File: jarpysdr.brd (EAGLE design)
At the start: 90 x 45 mm, 37 parts, among them IC1 74HC74N, IC2 NE5532N, IC3 7805, IC4 TL072P

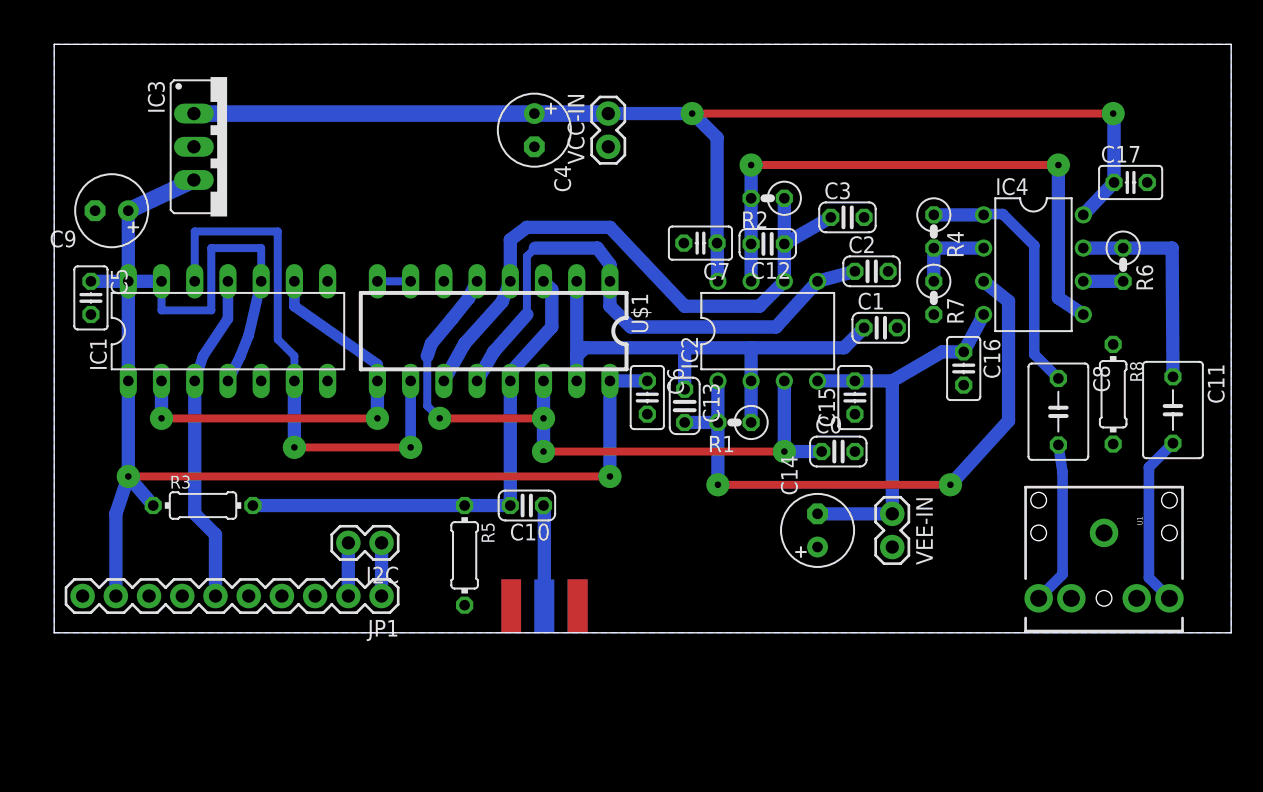
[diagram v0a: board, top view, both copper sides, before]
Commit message: Re-align all parts to a 0.1inch grid.
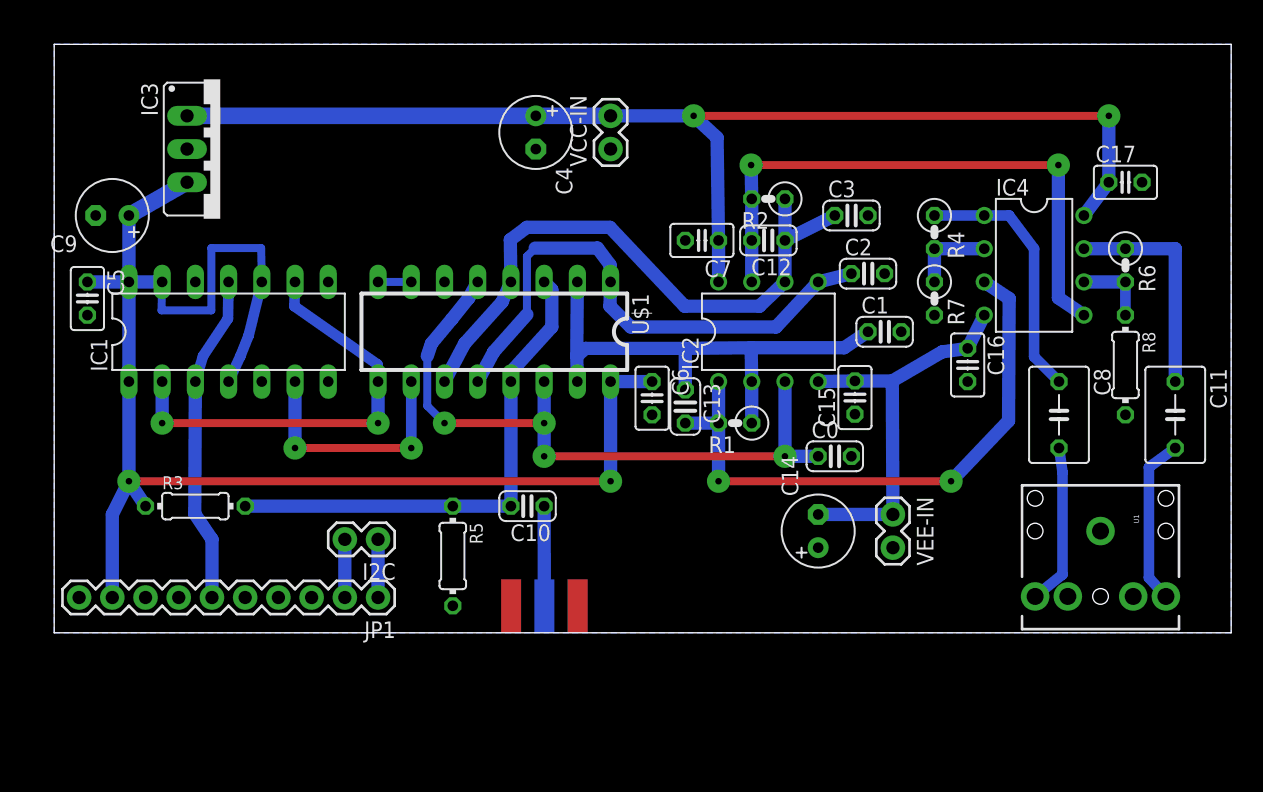
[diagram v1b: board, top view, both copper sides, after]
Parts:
- moved R8 2.43 mm to (81.9, 30.5)
- moved R5 0.91 mm to (30.5, 15.9)
- moved R3 0.59 mm to (10.8, 19.7)
- moved IC3 0.55 mm to (12.7, 47.0)
- moved C0 0.45 mm to (59.7, 23.5)
- moved C1 0.43 mm to (63.5, 33.0)
- moved C16 0.40 mm to (69.8, 30.5)
- moved C11 0.40 mm to (85.7, 26.7)
- moved C17 0.40 mm to (81.9, 44.5)
- moved I2C 0.38 mm to (24.8, 17.1)
- moved C9 0.37 mm to (4.45, 41.9)
- moved C6 0.37 mm to (45.7, 27.9)
- moved C3 0.33 mm to (61.0, 41.9)
- moved C2 0.32 mm to (62.2, 37.5)
- moved U1 0.31 mm to (80.0, 17.8)
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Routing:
- net N$3: track 41.2 -> 19.1 mm
- net N$15: track 3.05 -> 5.72 mm
- net N$2: track 33.2 -> 33.8 mm
- net N$4: track 38.3 -> 38.9 mm
- net +12V: track 92.8 -> 92.2 mm
- net N$13: track 16.6 -> 17.1 mm

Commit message: Double-sided layout.
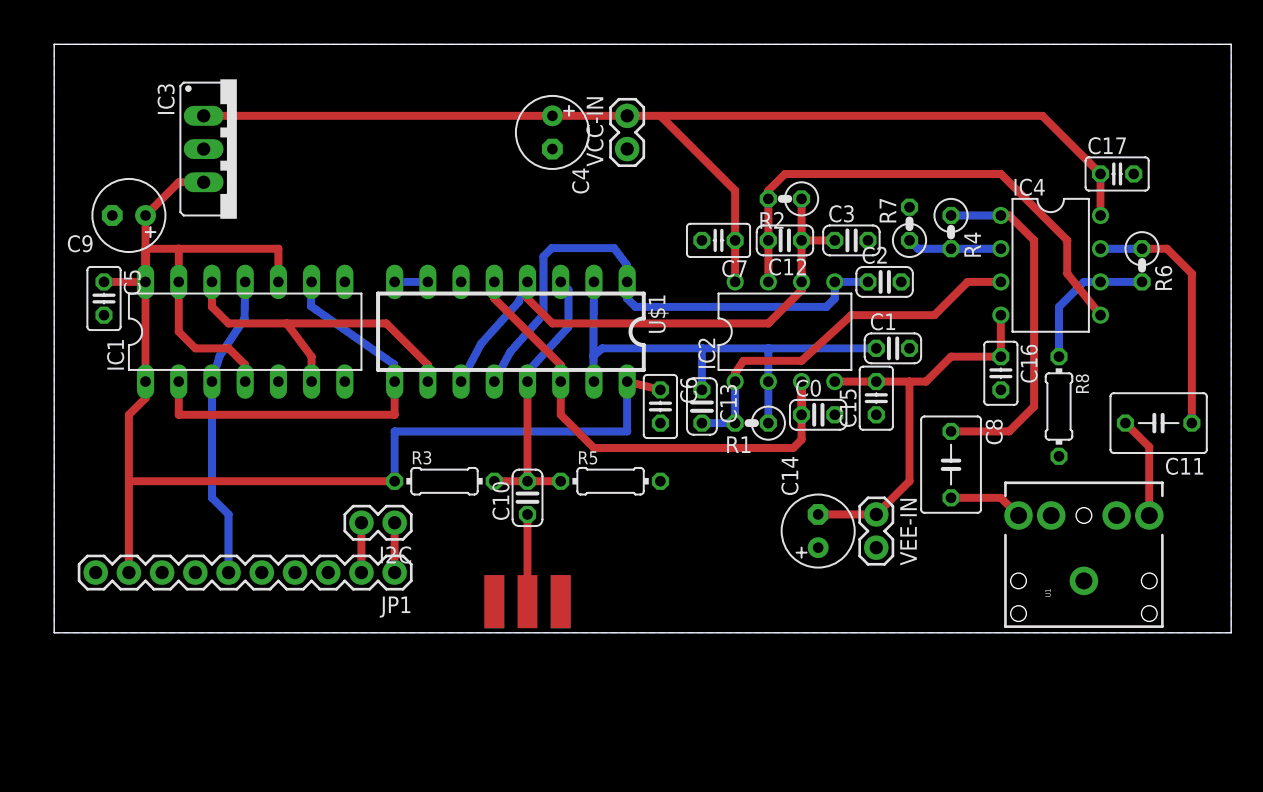
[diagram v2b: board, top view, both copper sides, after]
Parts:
- moved R3 19.1 mm to (29.8, 21.6)
- moved R5 13.4 mm to (42.5, 21.6), turned to 0 degrees
- moved C8 9.09 mm to (68.6, 22.9)
- moved R7 6.02 mm to (65.4, 41.3), turned to 90 degrees
- moved R8 5.99 mm to (76.8, 27.3)
- moved U1 4.02 mm to (78.7, 14.0), turned to 90 degrees
- moved J$1 3.81 mm to (38.7, 12.4), flipped to the top
- moved C0 3.42 mm to (58.4, 26.7)
- moved C16 2.62 mm to (72.4, 29.8)
- moved JP1 2.29 mm to (26.0, 14.6)
- moved C3 1.90 mm to (61.0, 40.0)
- moved I2C 1.80 mm to (26.0, 18.4)
- moved C15 1.64 mm to (62.9, 27.9)
- moved C1 1.42 mm to (64.1, 31.8)
- moved C2 1.42 mm to (63.5, 36.8)
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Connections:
- net GND: now also J$1.GND@2, J$1.GND@3
- net N$8: now also U1.TIP; no longer U1.RING
- net N$9: now also U1.RING; no longer U1.TIP
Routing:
- net N$4: track 38.9 -> 21.8 mm
- net N$6: track 46.0 -> 29.6 mm, vias 2 -> 0
- net N$5: track 52.6 -> 39.0 mm, vias 4 -> 0
- net N$3: track 19.1 -> 26.6 mm, vias 2 -> 0
- net N$11: track 19.8 -> 27.0 mm
- net N$9: track 12.4 -> 5.72 mm
- net N$10: track 44.9 -> 39.1 mm, vias 2 -> 0
- net N$15: track 5.72 -> 10.9 mm
- net N$8: track 12.9 -> 7.82 mm
- net N$14: track 47.7 -> 42.8 mm
- net +12V: track 92.2 -> 88.7 mm, vias 2 -> 0
- net N$13: track 17.1 -> 19.2 mm
- net CLK: track 25.2 -> 23.4 mm
- net +5V: track 115.5 -> 113.8 mm, vias 2 -> 0
- net -12V: track 30.8 -> 32.3 mm
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
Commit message: Move osc connector to left edge.
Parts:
- moved VCC-IN 42.3 mm to (1.59, 49.8)
- moved C4 30.6 mm to (7.62, 51.1)
- moved JP1 24.8 mm to (1.59, 19.1), turned to 90 degrees
- moved I2C 24.8 mm to (1.59, 14.3), turned to 270 degrees
- moved IC3 5.71 mm to (19.7, 47.0)
- moved C14 4.02 mm to (59.7, 21.6), turned to 0 degrees
- moved R5 3.62 mm to (44.8, 18.7)
- moved C10 3.43 mm to (38.1, 17.5)
- moved VEE-IN 3.17 mm to (64.8, 21.6)
- moved R3 2.13 mm to (31.8, 22.5), turned to 270 degrees
- moved C0 1.91 mm to (60.3, 26.7)
- moved C1 1.91 mm to (66.0, 31.8)
- moved C11 1.91 mm to (86.4, 26.0)
- moved C13 1.91 mm to (51.4, 27.3)
- moved C16 1.91 mm to (74.3, 29.8)
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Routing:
- net +12V: track 88.7 -> 101.6 mm
- net +5V: track 113.8 -> 103.5 mm
- net N$17: track 3.81 -> 13.7 mm
- net N$4: track 21.8 -> 28.8 mm
- net N$7: track 6.67 -> 3.81 mm
- net -12V: track 32.3 -> 30.6 mm
- net N$16: track 3.81 -> 4.76 mm
- net N$3: track 26.6 -> 26.0 mm
- net CLK: track 23.4 -> 22.9 mm

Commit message: Gave some love to the ground plane.
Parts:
- moved I2C 9.16 mm to (10.5, 12.1), turned to 0 degrees
- moved C16 3.59 mm to (71.8, 32.4), turned to 90 degrees
- moved C17 2.54 mm to (80.6, 45.1), turned to 180 degrees
- moved C3 1.59 mm to (61.9, 41.3), turned to 90 degrees
- moved C2 1.42 mm to (64.8, 38.1), turned to 90 degrees
- moved R7 1.14 mm to (68.3, 40.6)
- moved C6 0.71 mm to (48.6, 27.9)
- moved R4 0.64 mm to (71.1, 40.6)
- moved C13 0.64 mm to (51.4, 27.9)
- moved R1 0.64 mm to (55.2, 26.7)
- moved JP1 0.64 mm to (2.22, 19.1)
- moved VCC-IN 0.64 mm to (2.22, 49.8)
- moved C1 0.45 mm to (65.7, 32.1)
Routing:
- net N$16: track 4.76 -> 12.1 mm
- net N$1: track 40.8 -> 45.9 mm
- net N$17: track 13.7 -> 16.0 mm
- net -12V: track 30.6 -> 29.0 mm
- net N$12: track 7.25 -> 6.03 mm
- net N$14: track 42.8 -> 43.9 mm
- net C-180DEG: track 38.4 -> 37.4 mm
- net N$5: track 39.0 -> 39.7 mm
- net N$11: track 27.0 -> 26.3 mm
- net N$6: track 29.6 -> 29.0 mm
- net CLK: track 22.9 -> 22.2 mm
- net +12V: track 101.6 -> 101.0 mm

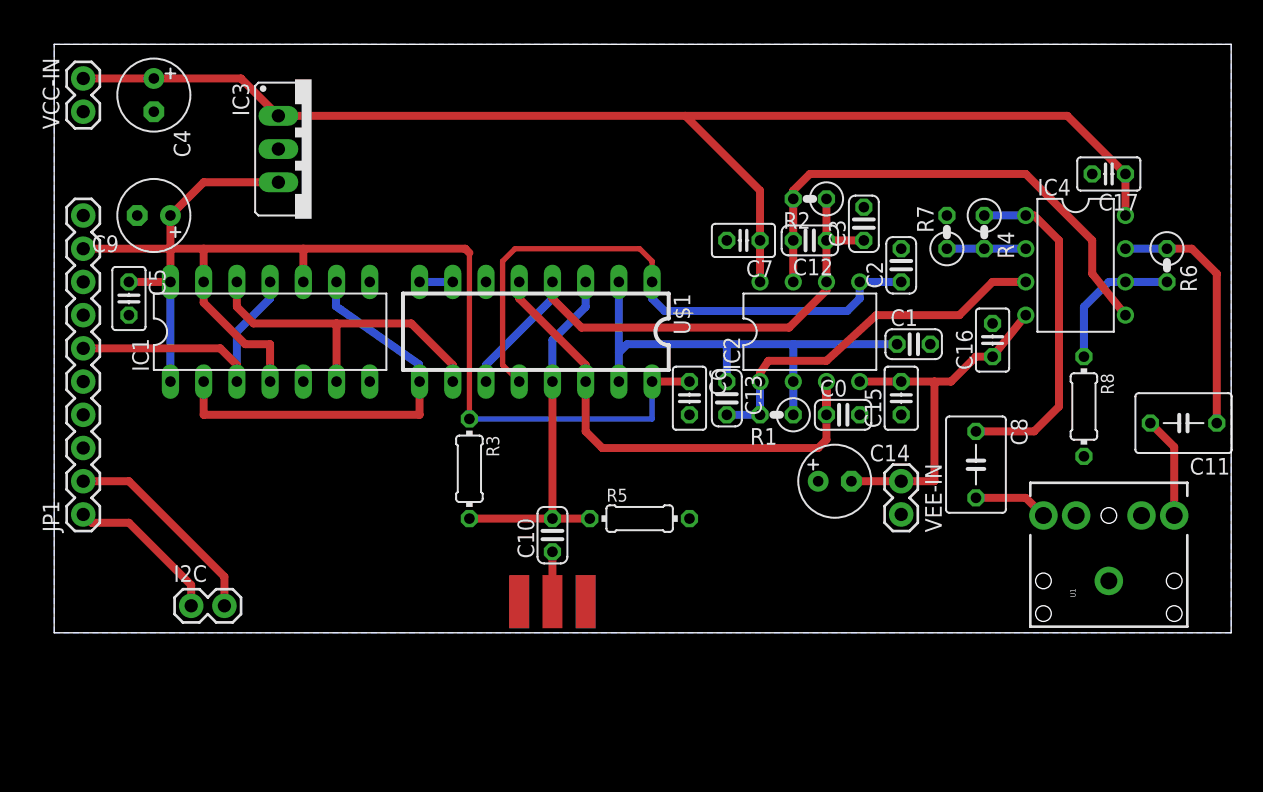
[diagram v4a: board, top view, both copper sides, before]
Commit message: Added power planes.
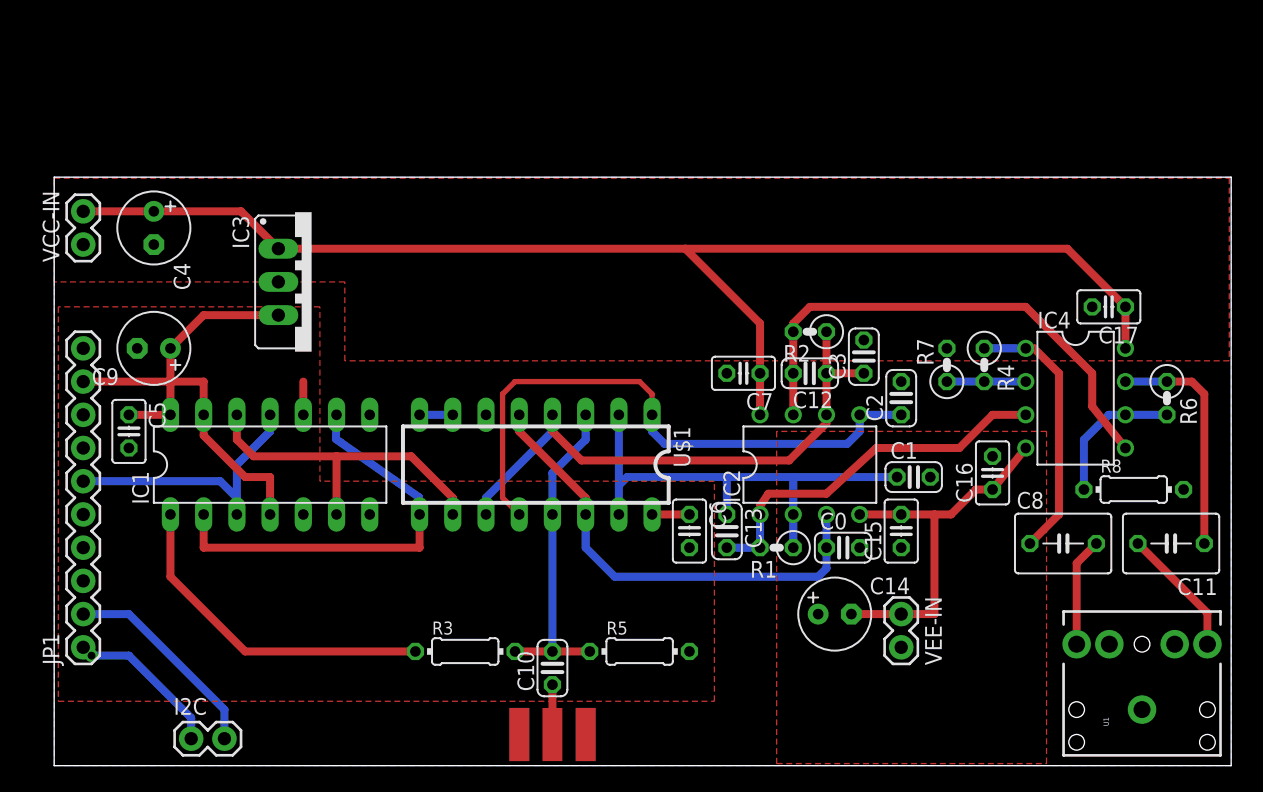
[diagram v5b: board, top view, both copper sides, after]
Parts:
- moved R3 14.0 mm to (31.4, 8.57), turned to 0 degrees
- moved U1 10.2 mm to (83.2, 4.13)
- moved C1 10.2 mm to (65.7, 21.9)
- moved C12 10.2 mm to (57.8, 29.8)
- moved C17 10.2 mm to (80.6, 34.9)
- moved C5 10.2 mm to (5.71, 25.4)
- moved C7 10.2 mm to (52.7, 29.8)
- moved IC1 10.2 mm to (16.5, 22.9)
- moved IC2 10.2 mm to (57.8, 22.9)
- moved IC3 10.2 mm to (19.7, 36.8)
- moved U$1 10.2 mm to (36.8, 22.9)
- moved R5 10.2 mm to (44.8, 8.57)
- moved C0 10.2 mm to (60.3, 16.5)
- moved C13 10.2 mm to (51.4, 17.8)
- moved C14 10.2 mm to (59.7, 11.4)
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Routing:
- net +5V: track 103.1 -> 71.4 mm
- net N$11: track 26.3 -> 20.4 mm
- net N$5: track 39.7 -> 36.0 mm
- net N$4: track 28.4 -> 24.9 mm
- net N$9: track 5.72 -> 8.32 mm
- net N$8: track 7.82 -> 9.90 mm
- net N$13: track 19.2 -> 17.9 mm
- net N$16: vias 0 -> 1
- added copper zone on layer 1, net +12V
- added copper zone on layer 1, net +5V
- added copper zone on layer 1, net -12V
